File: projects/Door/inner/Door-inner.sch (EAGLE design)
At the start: 28 parts, among them IC1 7815TV, J2 AVR_SPI_PROG_3X2PTH, J3 LCD, U2 LP2985-33DBVR, X1 POWERSUPPLY_DC21MMX, Y1 16MHz

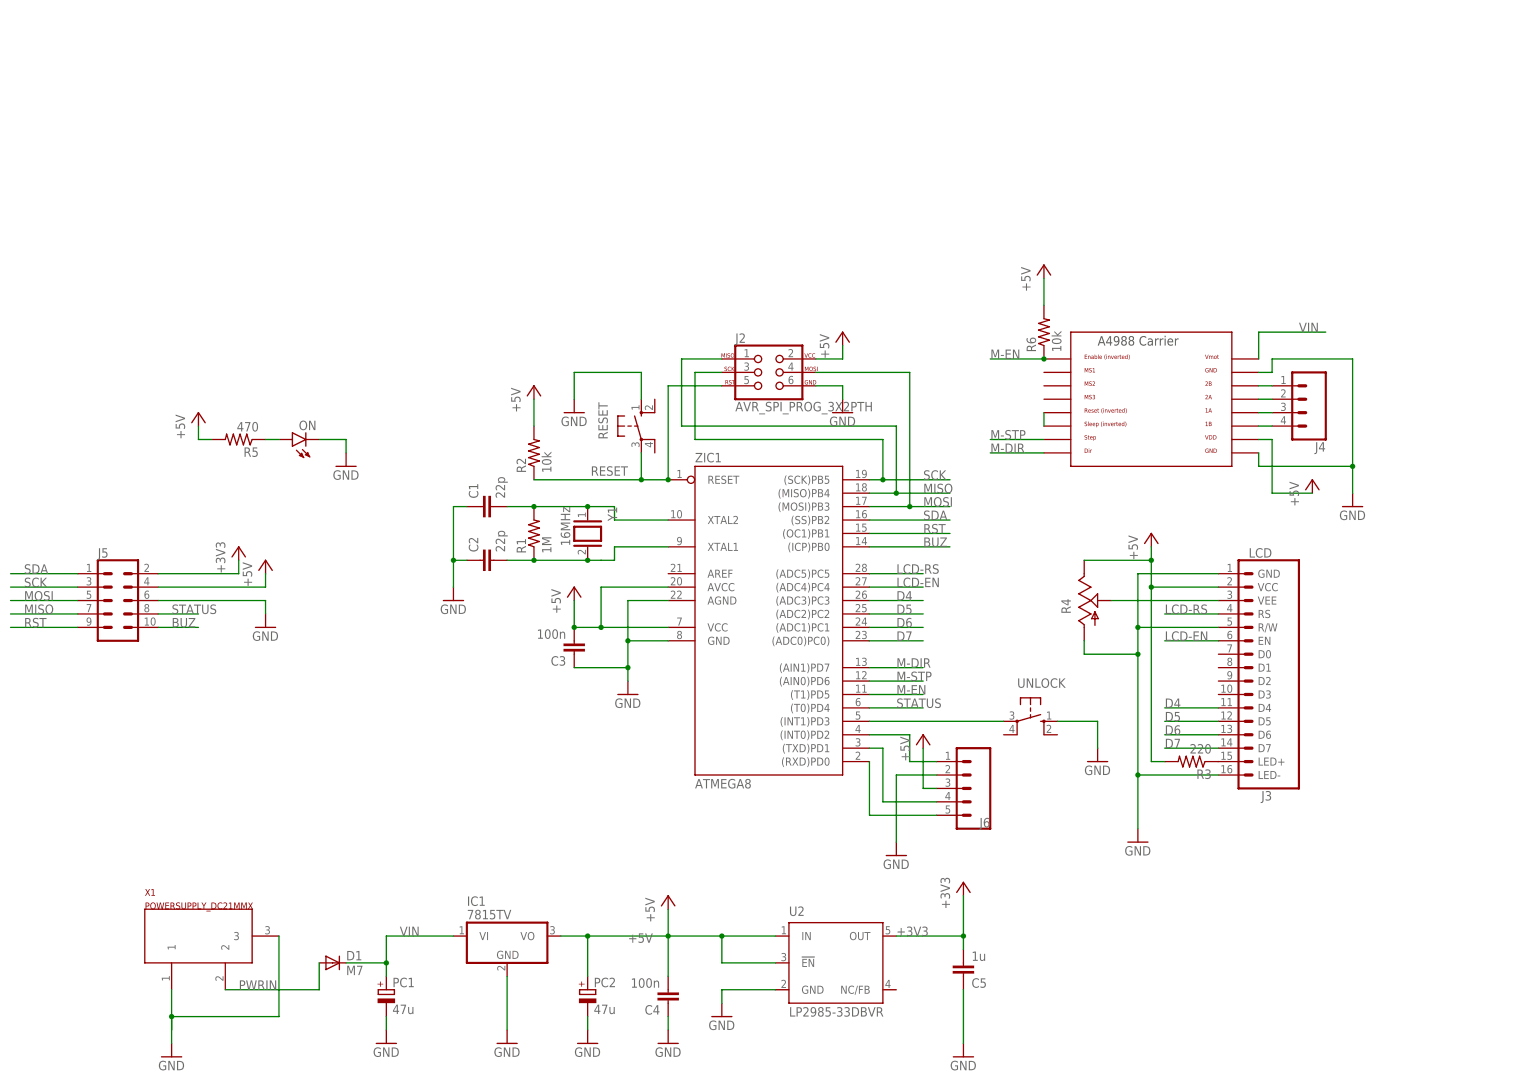
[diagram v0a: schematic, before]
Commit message: Rerouted door boards for rivet-plated vias instead of plated through-holes
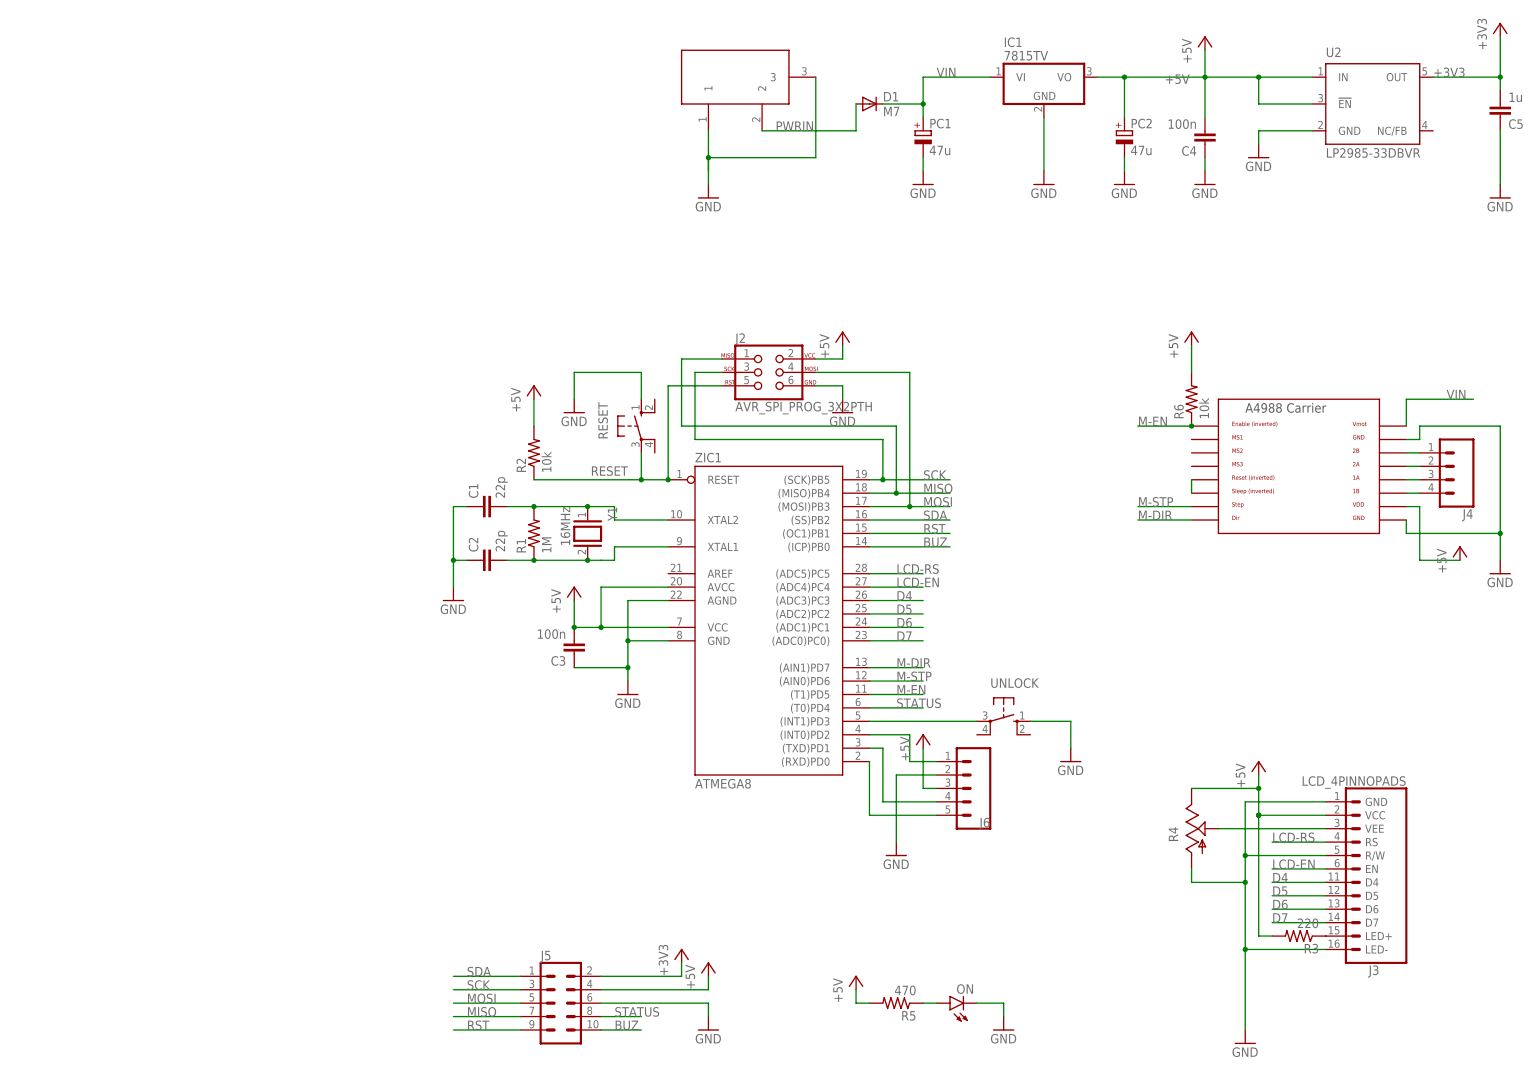
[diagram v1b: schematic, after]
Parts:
- J3: value LCD -> LCD_4PINNOPADS; device lcd:LCD -> lcd:LCD_4PINNOPADS
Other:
- note added: "Control"
- note added: "Door"
- note added: "LCD"
- note added: "LED"
- note added: "Microcontroller"
- note added: "Motor"
- note added: "Output"
- note added: "Panel"
- note added: "Power"
- moved on the sheet: C4, C5, D1, IC1, J4, J5, ON, PC1, PC2, R3, R4, R5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

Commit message: Via rivets apparently have a 0.6mm INNER diameter
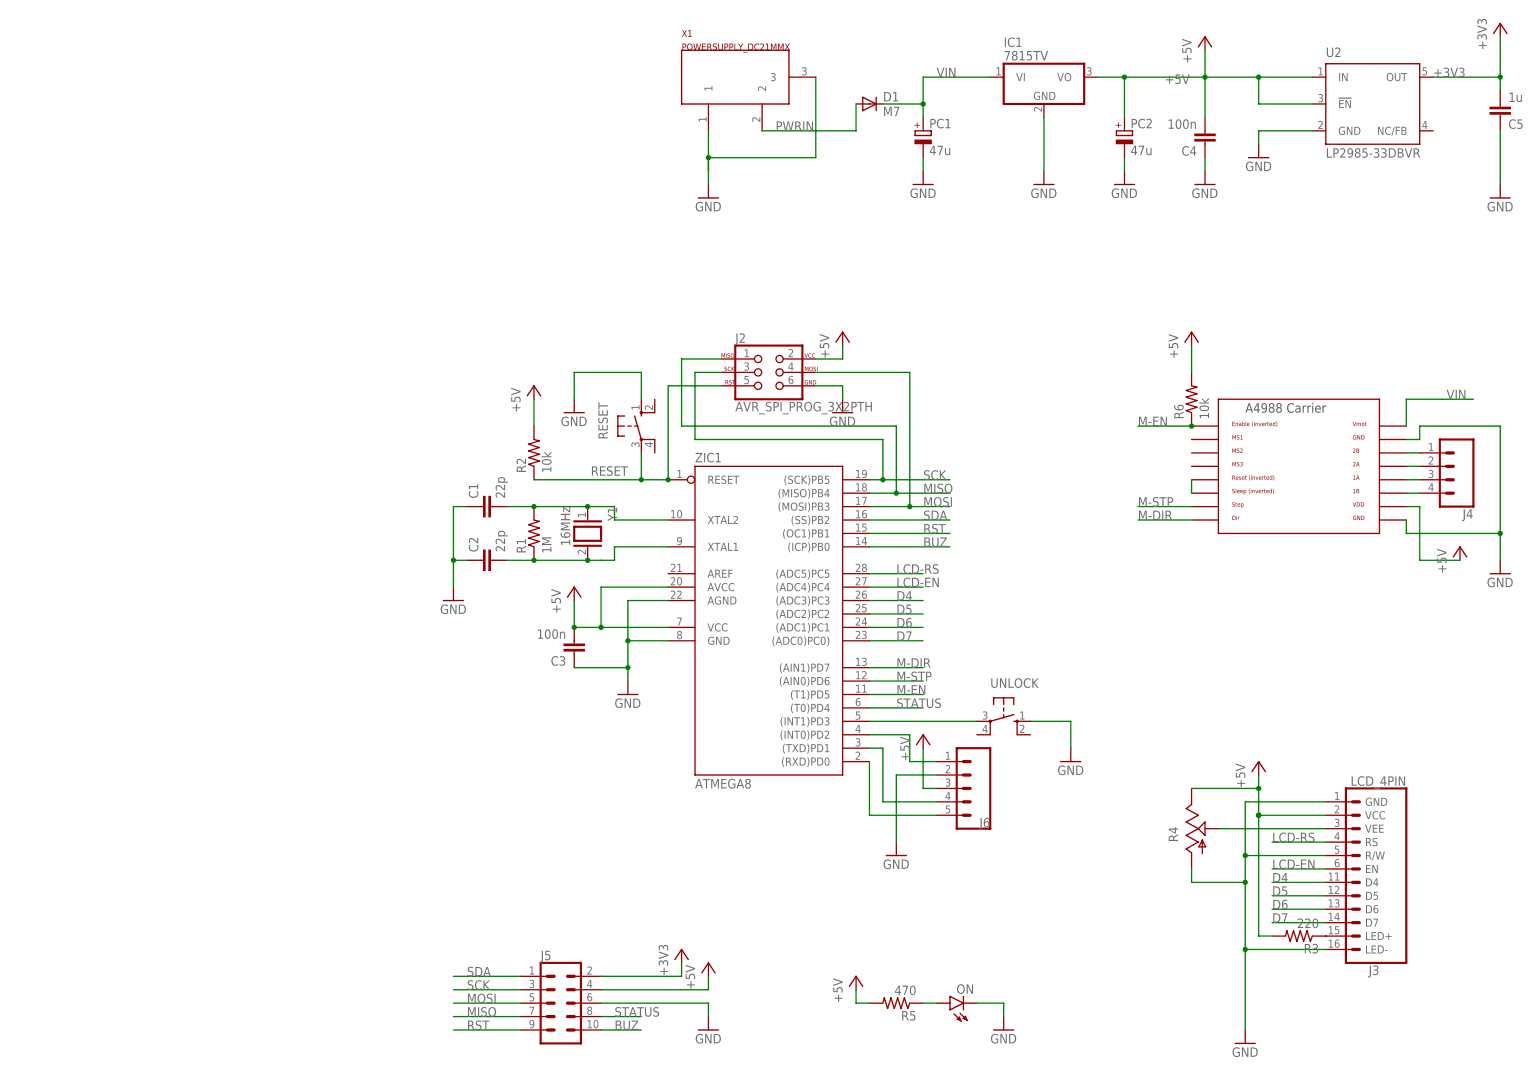
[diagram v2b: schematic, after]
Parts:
- J3: value LCD_4PINNOPADS -> LCD_4PIN; device lcd:LCD_4PINNOPADS -> lcd:LCD_4PIN

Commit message: Door-inner redesign
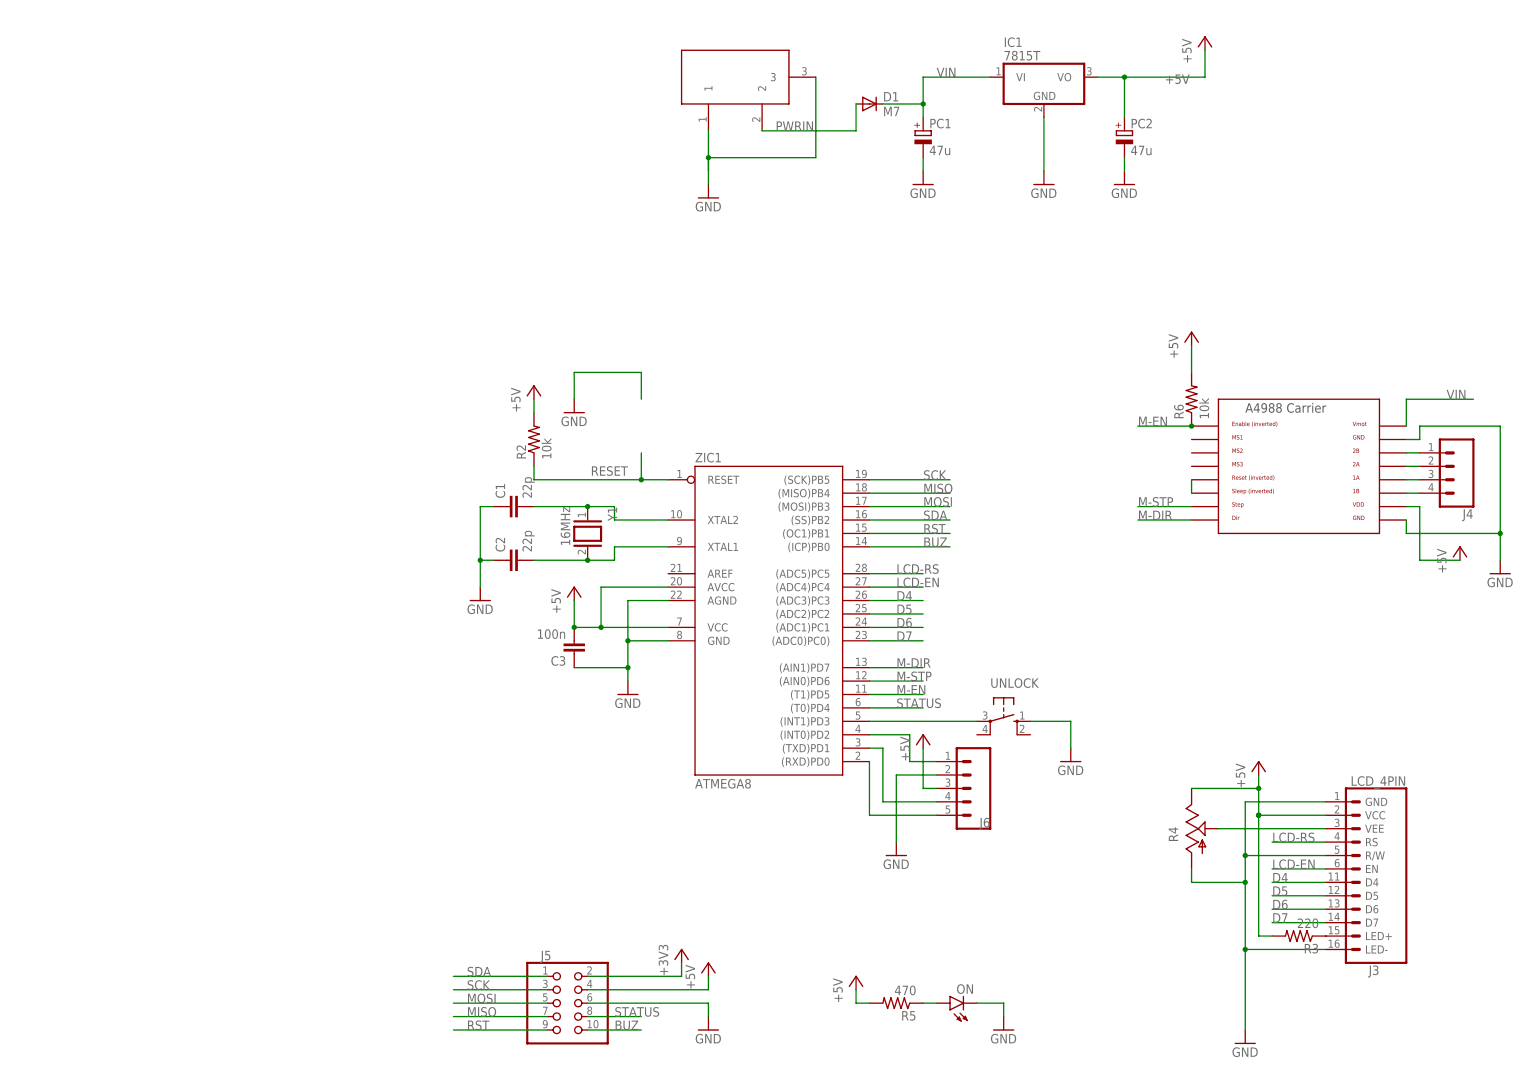
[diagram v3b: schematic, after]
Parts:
- removed C4: 100n, SmartPrj:C-EUC0805
- removed C5: 1u, SmartPrj:C-EUC0805
- removed J2: AVR_SPI_PROG_3X2PTH, SparkFun-Connectors:AVR_SPI_PROG_3X2PTH
- removed R1: 1M, resistor:R-US_R0805
- removed RESET: (no value), switch-omron:10-XX
- removed U2: LP2985-33DBVR, texas:TPS77033
- C1, C2: device resistor:C-EUC0805 -> resistor:C-EU025-030X050
- C3: device resistor:C-EUC0805 -> resistor:C-EU050-030X075
- D1: device diode:DIODE-SMB -> diode:DIODE-D-7.5
- IC1: value 7815TV -> 7815T; device linear:7815TV -> linear:7815T
- J5: device SparkFun-Connectors:CONN_05X2PTH -> pinhead:PINHD-2X5
- ON: device led:LEDCHIPLED_0805 -> led:LED3MM
- R2, R3, R5, R6: device resistor:R-US_R0805 -> resistor:R-US_0207/10
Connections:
- net +3V3: no longer C5.2, U2.OUT
- net +5V: no longer C4.2, J2.2, U2.!EN, U2.IN
- net GND: no longer C4.1, C5.1, J2.6, RESET.S, U2.GND
- net MISO: no longer J2.1
- net MOSI: no longer J2.4
- net RESET: no longer J2.5, RESET.P
- net SCK: no longer J2.3
- net XTAL1: no longer R1.1
- net XTAL2: no longer R1.2
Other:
- moved on the sheet: C1, C2, R2

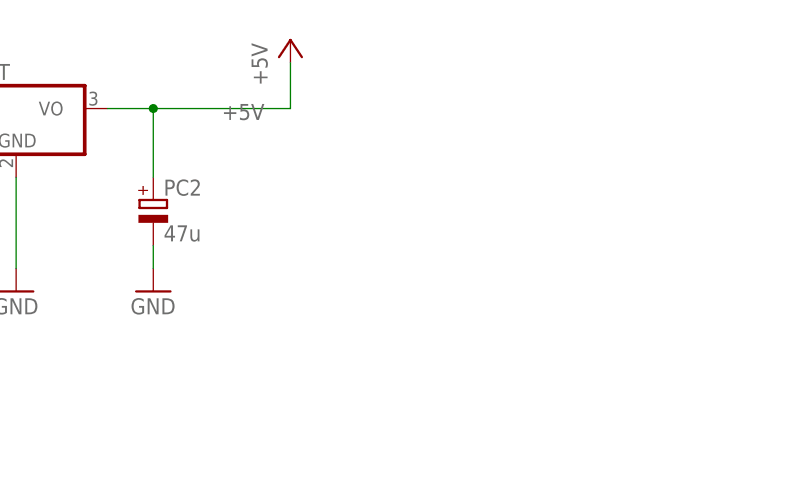
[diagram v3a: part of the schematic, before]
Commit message: Extra vias in inner door
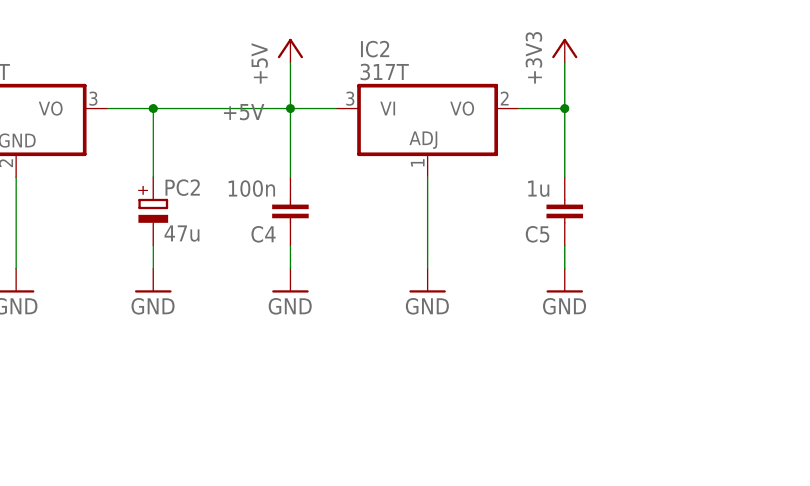
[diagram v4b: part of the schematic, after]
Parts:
- added C4: 100n, resistor:C-EU050-030X075
- added C5: 1u, resistor:C-EU050-030X075
- added IC2: 317T, linear:317T
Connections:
- net +3V3: now also C5.2, IC2.VO
- net +5V: now also C4.2, IC2.VI
- net GND: now also C4.1, C5.1, IC2.ADJ
